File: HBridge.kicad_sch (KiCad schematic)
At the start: 0 parts

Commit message: HBridge stuff
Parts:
- added 0.1uF1: C3, symbol Device:C_Small
- added 1.5ohms1, 1.5ohms2: Raisen, symbol Device:R_Small
- added 10kohm1: R_Small, symbol Device:R_Small
- added 10uF1: C2, symbol Device:C_Small
- added 2.2uF1: C1, symbol Device:C_Small
- added J1, J2: Conn_01x02_Pin, symbol Connector:Conn_01x02_Pin
- added J3: Conn_01x07_Pin, symbol Connector:Conn_01x07_Pin
- added U1: DRV8848PWP, PWP0016C_N, symbol DDRV8848:DRV8848PWP
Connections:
- new net: J1.1 (Pin_1), U1.2 (AOUT1)
- new net: J1.2 (Pin_2), U1.4 (AOUT2)
- new net: 1.5ohms1.2, U1.6 (BISEN)
- new net: 2.2uF1.1, U1.11 (VREF), U1.14 (VINT)
- new net: 10kohm1.1, U1.8 (FAULT_N)
- new net: 10kohm1.2, J3.2 (Pin_2)
- new net: J3.1 (Pin_1), U1.1 (SLEEP_N)
- new net: J3.4 (Pin_4), U1.10 (BIN2)
- new net: J3.5 (Pin_5), U1.15 (AIN2)
- new net: J3.6 (Pin_6), U1.16 (AIN1)
- new net: 1.5ohms2.2, U1.3 (AISEN)
- new net: J2.1 (Pin_1), U1.5 (BOUT2)
- new net: J2.2 (Pin_2), U1.7 (BOUT1)
- new net: J3.3 (Pin_3), U1.9 (BIN1)
- new net +12V: 0.1uF1.2, 10uF1.2, U1.12 (VM)
- new net GND: 0.1uF1.1, 1.5ohms1.1, 1.5ohms2.1, 10uF1.1, 2.2uF1.2, J3.7 (Pin_7), U1.13 (GND), U1.17 (PAD)

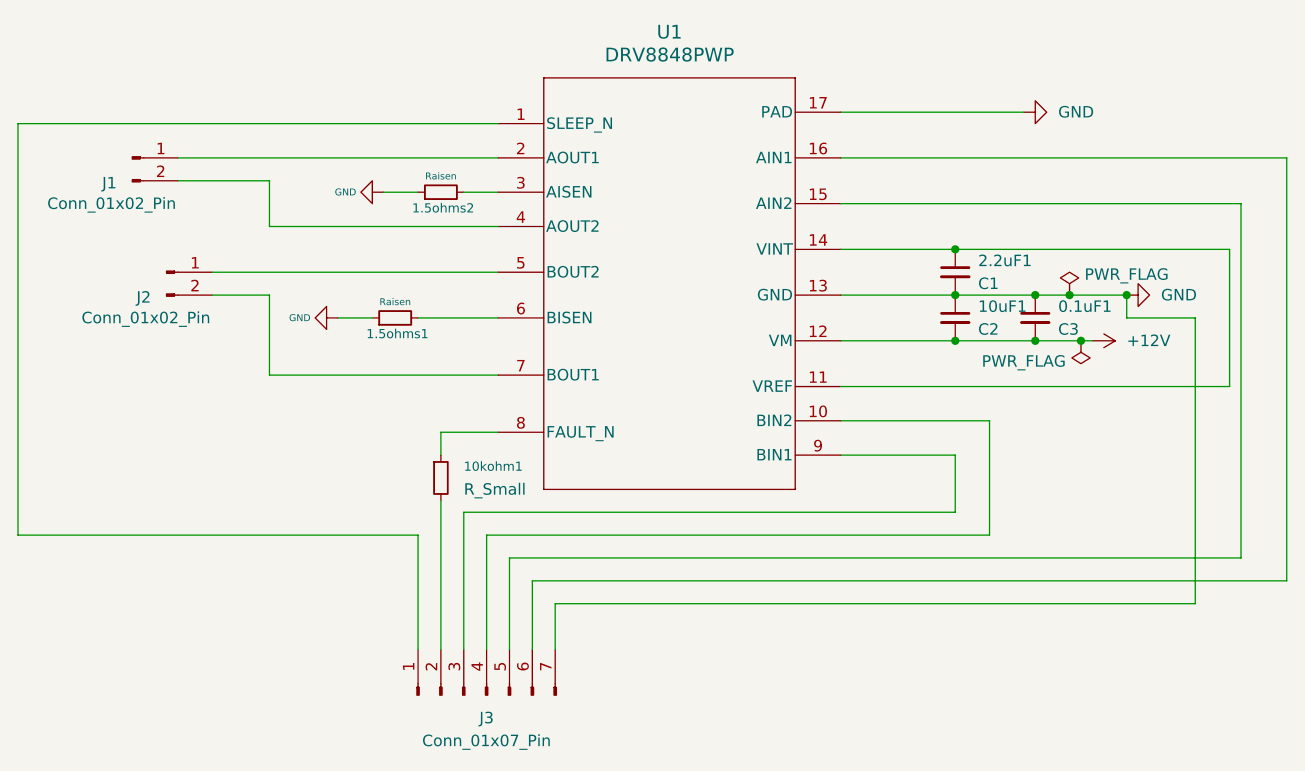
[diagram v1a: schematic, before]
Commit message: HBridge top file connections (NOT CONNECTED TO TOP FILE YET)
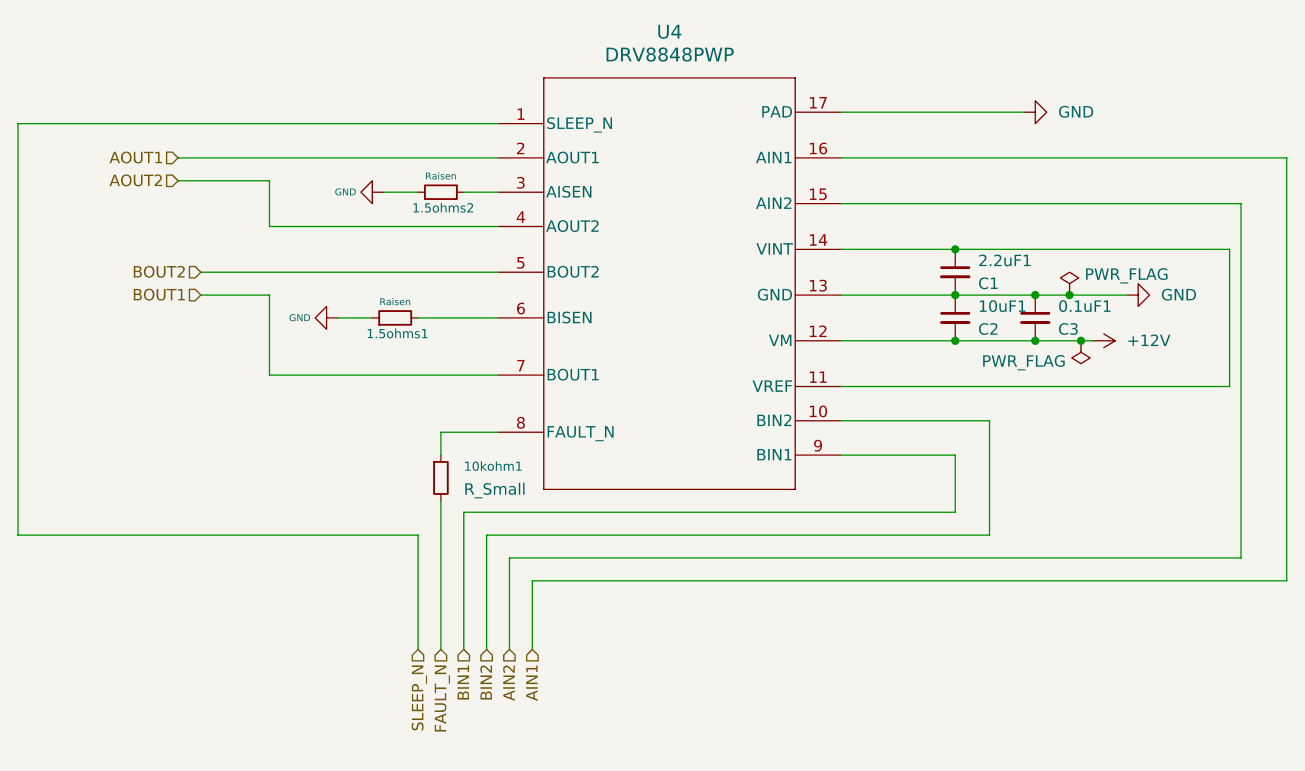
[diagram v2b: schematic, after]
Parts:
- removed J1, J2: Conn_01x02_Pin, symbol Connector:Conn_01x02_Pin
- removed J3: Conn_01x07_Pin, symbol Connector:Conn_01x07_Pin
- renumbered U1 to U4
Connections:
- net AOUT1: now reaches U4.2 (AOUT1)
- net AOUT2: now reaches U4.4 (AOUT2)
- net FAULT_N: now reaches 10kohm1.2
- net SLEEP_N: now reaches U4.1 (SLEEP_N)
- net BIN2: now reaches U4.10 (BIN2)
- net AIN2: now reaches U4.15 (AIN2)
- net AIN1: now reaches U4.16 (AIN1)
- net BOUT2: now reaches U4.5 (BOUT2)
- net BOUT1: now reaches U4.7 (BOUT1)
- net BIN1: now reaches U4.9 (BIN1)

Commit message: Added footprints
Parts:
- 0.1uF1: footprint (none) -> Capacitor_SMD:C_0805_2012Metric
- 1.5ohms1, 1.5ohms2: footprint (none) -> Resistor_SMD:R_1210_3225Metric
- 10kohm1: footprint (none) -> Resistor_SMD:R_0805_2012Metric
- 10uF1: footprint (none) -> Capacitor_SMD:C_1206_3216Metric
- 2.2uF1: footprint (none) -> Capacitor_SMD:C_1210_3225Metric
- U4: footprint PWP0016C_N -> (none)
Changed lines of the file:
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@@
 			)
 		)
-		(property "Footprint" ""
+		(property "Footprint" "Capacitor_SMD:C_1206_3216Metric"
 			(at 147.32 73.66 0)
 			(effects
@@
 			)
 		)
-		(property "Footprint" ""
+		(property "Footprint" "Resistor_SMD:R_1210_3225Metric"
 			(at 85.09 73.66 0)
 			(effects
@@
 			)
 		)
-		(property "Footprint" ""
+		(property "Footprint" "Capacitor_SMD:C_0805_2012Metric"
 			(at 156.21 73.66 0)
 			(effects
@@
 			)
 		)
-		(property "Footprint" ""
+		(property "Footprint" "Capacitor_SMD:C_1210_3225Metric"
 			(at 147.32 68.58 0)
 			(effects
@@
 			)
 		)
-		(property "Footprint" ""
+		(property "Footprint" "Resistor_SMD:R_0805_2012Metric"
 			(at 90.17 91.44 0)
 			(effects
@@
 			)
 		)
-		(property "Footprint" "PWP0016C_N"
+		(property "Footprint" ""
 			(at 114.3 69.85 0)
 			(effects
@@
 			)
 		)
-		(property "Footprint" ""
+		(property "Footprint" "Resistor_SMD:R_1210_3225Metric"
 			(at 90.17 59.69 0)
 			(effects

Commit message: ICs added
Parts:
- U4: footprint (none) -> DRV8848PWP:IC_DRV8848PWP
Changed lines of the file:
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@@
 			)
 		)
-		(property "Footprint" ""
+		(property "Footprint" "DRV8848PWP:IC_DRV8848PWP"
 			(at 114.3 69.85 0)
 			(effects
